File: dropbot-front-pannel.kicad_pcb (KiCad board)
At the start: 2 copper layers, 108.3 x 68.8 mm, 11 parts, among them J1 TFM-120-02-X-DH, J2 TFM-125-02-X-DH, J3 TFM-120-02-X-DH, P1 CONN_02X10, P2 CONN_02X25, P4 CONN_02X25, P6 CONN_02X25, P8 CONN_02X10, P9 CONN_01X03

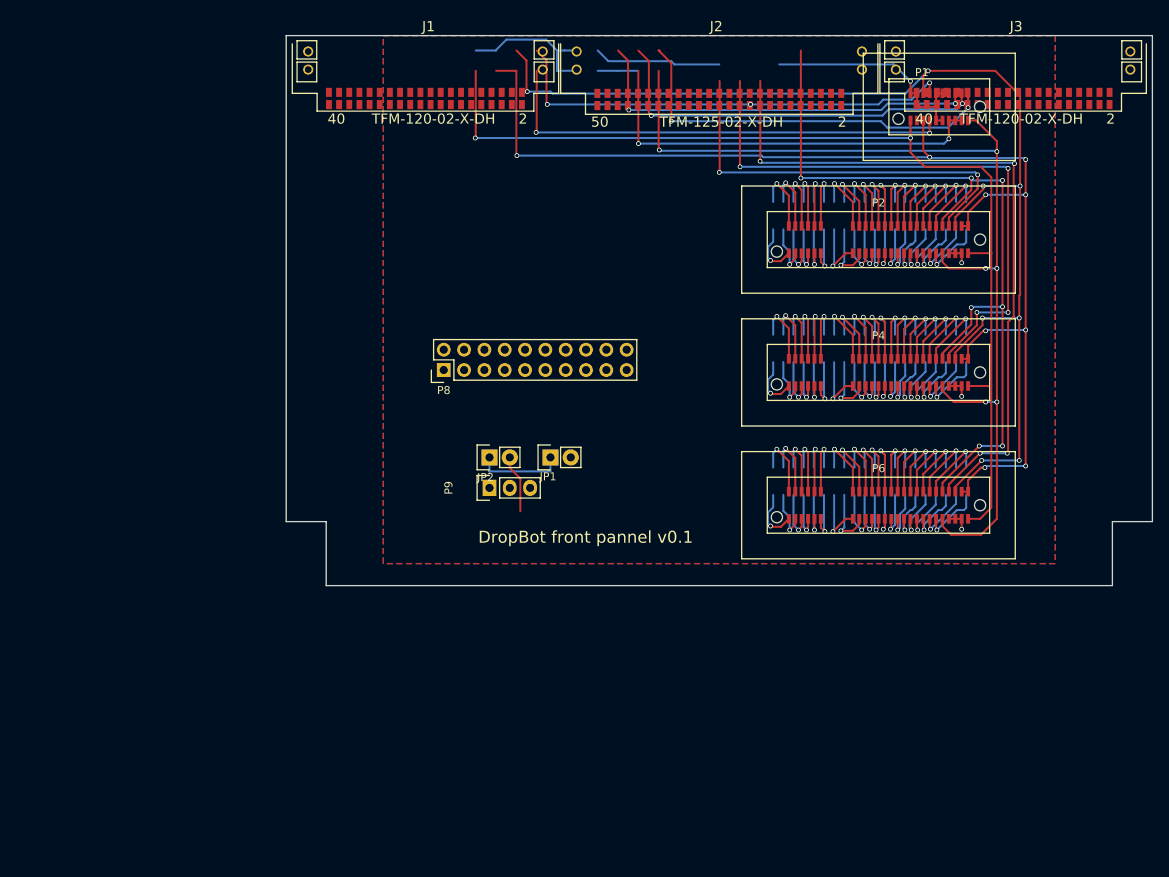
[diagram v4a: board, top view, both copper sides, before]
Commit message: [WIP] Update to use new Samtec connectors...
* add USB passthrough
* add 3.3V power regulator
* add reverse polarity protection on +12V power line
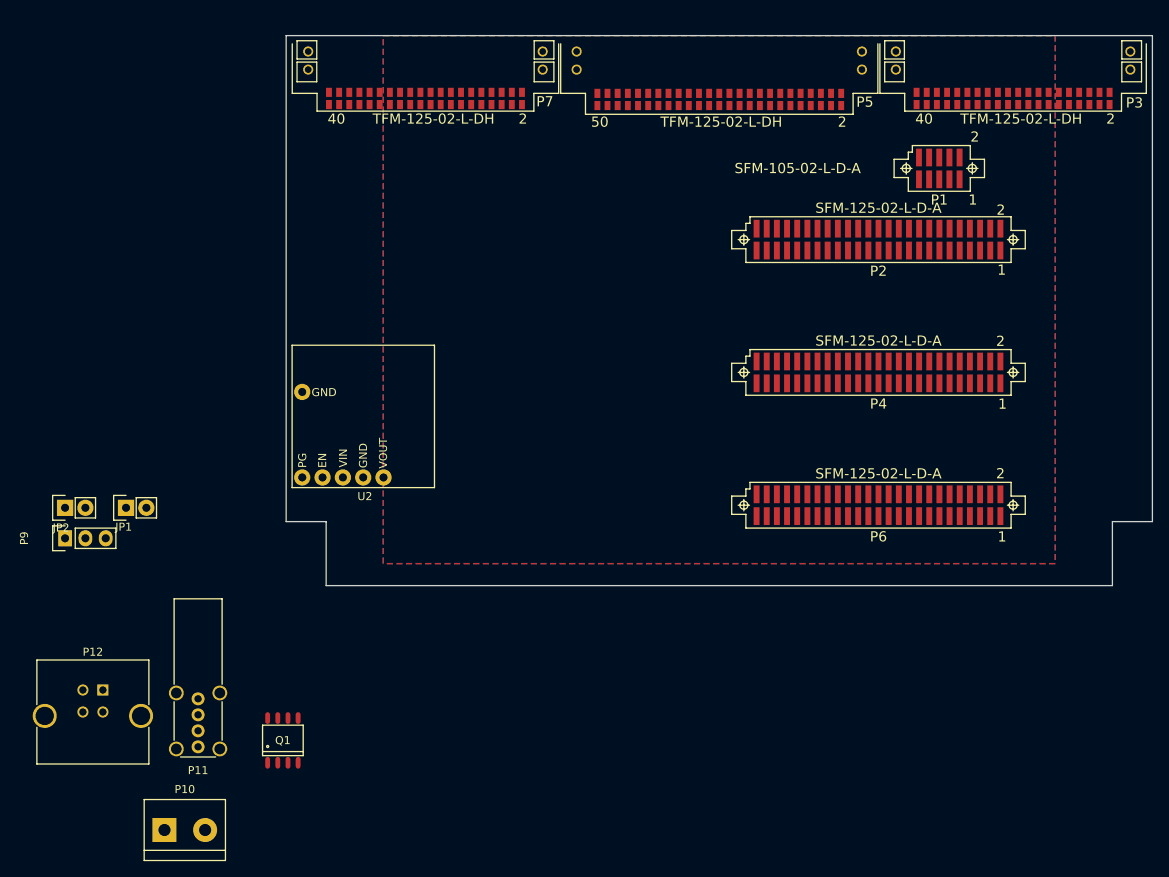
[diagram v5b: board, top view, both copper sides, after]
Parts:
- removed P8: CONN_02X10, Pin_Headers:Pin_Header_Straight_2x10
- added P10: CONN_01X02, Connect:bornier2, F.Cu at (-69.3, 120.3)
- added P11: USB_A, Connect:USB_A_Vertical, F.Cu at (-65.2, 103.9)
- added P12: USB_B, Connect:USB_B_MUSB_Straight, F.Cu at (-77.0, 102.8)
- added Q1: IRF9388TRPBF, Power_Integrations:SO-8, F.Cu at (-54.5, 109.1)
- added U2: D24V22F3, WheelerLab:D24V22F, F.Cu at (-53.4, 77.5)
- P1: value CONN_02X10 -> SFM-105-02-L-D-A; footprint WheelerLab:HSEC8-110-XX-X-DV -> WheelerLab:SFM-105-02-XXX-D-A
- P2, P4, P6: value CONN_02X25 -> SFM-125-02-L-D-A; footprint WheelerLab:HSEC8-125-XX-X-DV -> WheelerLab:SFM-125-02-XXX-D-A
- P3: renamed from J3; value TFM-120-02-X-DH -> TFM-125-02-L-DH
- P5: renamed from J2; value TFM-125-02-X-DH -> TFM-125-02-L-DH
- P7: renamed from J1; value TFM-120-02-X-DH -> TFM-125-02-L-DH
- moved JP1 53.4 mm to (-74.2, 80.0)
- moved JP2 53.4 mm to (-81.8, 80.0)
- moved P9 53.4 mm to (-81.8, 83.8)
- moved P1 7.70 mm to (27.5, 37.6)
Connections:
- P1 pad 10: GND -> HVAC
- P1 pad 4: GND -> SCL
- P1 pad 5: +3.3V -> CUR_SENSE
- P1 pad 6: SCL -> GND
- P1 pad 7: CUR_SENSE -> +12V
- P1 pad 9: GND -> +12V
- P3 pad 1: Net-(J3-Pad1) -> HVOUT0
- P3 pad 10: Net-(J3-Pad10) -> HVOUT9
- P3 pad 11: Net-(J3-Pad11) -> HVOUT10
- P3 pad 12: Net-(J3-Pad12) -> HVOUT11
- P3 pad 13: Net-(J3-Pad13) -> HVOUT12
- P3 pad 14: Net-(J3-Pad14) -> HVOUT13
- P3 pad 15: Net-(J3-Pad15) -> HVOUT14
- P3 pad 16: Net-(J3-Pad16) -> HVOUT15
- P3 pad 17: Net-(J3-Pad17) -> HVOUT16
- P3 pad 18: Net-(J3-Pad18) -> HVOUT17
- P3 pad 19: Net-(J3-Pad19) -> HVOUT18
- P3 pad 2: Net-(J3-Pad2) -> HVOUT1
- P3 pad 20: Net-(J3-Pad20) -> HVOUT19
- P3 pad 21: Net-(J3-Pad21) -> HVOUT20
- P3 pad 22: Net-(J3-Pad22) -> HVOUT21
- P3 pad 23: Net-(J3-Pad23) -> HVOUT22
- P3 pad 24: Net-(J3-Pad24) -> HVOUT23
- P3 pad 25: Net-(J3-Pad25) -> HVOUT24
- P3 pad 26: Net-(J3-Pad26) -> HVOUT25
- P3 pad 27: Net-(J3-Pad27) -> HVOUT26
- P3 pad 28: Net-(J3-Pad28) -> HVOUT27
- P3 pad 29: Net-(J3-Pad29) -> HVOUT28
- P3 pad 3: Net-(J3-Pad3) -> HVOUT2
- P3 pad 30: Net-(J3-Pad30) -> HVOUT29
- P3 pad 31: Net-(J3-Pad31) -> HVOUT30
- P3 pad 32: Net-(J3-Pad32) -> HVOUT31
- P3 pad 33: Net-(J3-Pad33) -> HVOUT32
- P3 pad 34: Net-(J3-Pad34) -> HVOUT33
- P3 pad 35: Net-(J3-Pad35) -> HVOUT34
- P3 pad 36: Net-(J3-Pad36) -> HVOUT35
- P3 pad 37: Net-(J3-Pad37) -> HVOUT36
- P3 pad 38: Net-(J3-Pad38) -> HVOUT37
- P3 pad 39: Net-(J3-Pad39) -> HVOUT38
- P3 pad 4: Net-(J3-Pad4) -> HVOUT3
- P3 pad 40: Net-(J3-Pad40) -> HVOUT39
- P3 pad 5: Net-(J3-Pad5) -> HVOUT4
- P3 pad 6: Net-(J3-Pad6) -> HVOUT5
- P3 pad 7: Net-(J3-Pad7) -> HVOUT6
- P3 pad 8: Net-(J3-Pad8) -> HVOUT7
- P3 pad 9: Net-(J3-Pad9) -> HVOUT8
- P5 pad 1: Net-(J2-Pad1) -> HVOUT40
- P5 pad 10: Net-(J2-Pad10) -> HVOUT49
- P5 pad 11: Net-(J2-Pad11) -> HVOUT50
- P5 pad 12: Net-(J2-Pad12) -> HVOUT51
- P5 pad 13: Net-(J2-Pad13) -> HVOUT52
- P5 pad 14: Net-(J2-Pad14) -> HVOUT53
- P5 pad 15: Net-(J2-Pad15) -> HVOUT54
- P5 pad 16: Net-(J2-Pad16) -> HVOUT55
- P5 pad 17: Net-(J2-Pad17) -> HVOUT56
- P5 pad 18: Net-(J2-Pad18) -> HVOUT57
- P5 pad 19: Net-(J2-Pad19) -> HVOUT58
- P5 pad 2: Net-(J2-Pad2) -> HVOUT41
- P5 pad 20: Net-(J2-Pad20) -> HVOUT59
- P5 pad 21: Net-(J2-Pad21) -> HVOUT60
- P5 pad 22: Net-(J2-Pad22) -> HVOUT61
- P5 pad 23: Net-(J2-Pad23) -> HVOUT62
- P5 pad 24: Net-(J2-Pad24) -> HVOUT63
- P5 pad 25: Net-(J2-Pad25) -> HVOUT64
- P5 pad 26: Net-(J2-Pad26) -> HVOUT65
- P5 pad 27: Net-(J2-Pad27) -> HVOUT66
- P5 pad 28: Net-(J2-Pad28) -> HVOUT67
- P5 pad 29: Net-(J2-Pad29) -> HVOUT68
- P5 pad 3: Net-(J2-Pad3) -> HVOUT42
- P5 pad 30: Net-(J2-Pad30) -> HVOUT69
- P5 pad 31: Net-(J2-Pad31) -> HVOUT70
- P5 pad 32: Net-(J2-Pad32) -> HVOUT71
- P5 pad 33: Net-(J2-Pad33) -> HVOUT72
- P5 pad 34: Net-(J2-Pad34) -> HVOUT73
- P5 pad 35: Net-(J2-Pad35) -> HVOUT74
- P5 pad 36: Net-(J2-Pad36) -> HVOUT75
- P5 pad 37: Net-(J2-Pad37) -> HVOUT76
- P5 pad 38: Net-(J2-Pad38) -> HVOUT77
- P5 pad 39: Net-(J2-Pad39) -> HVOUT78
- P5 pad 4: Net-(J2-Pad4) -> HVOUT43
- P5 pad 40: Net-(J2-Pad40) -> HVOUT79
- P5 pad 5: Net-(J2-Pad5) -> HVOUT44
- P5 pad 6: Net-(J2-Pad6) -> HVOUT45
- P5 pad 7: Net-(J2-Pad7) -> HVOUT46
- P5 pad 8: Net-(J2-Pad8) -> HVOUT47
- P5 pad 9: Net-(J2-Pad9) -> HVOUT48
- P7 pad 1: Net-(J1-Pad1) -> HVOUT80
- P7 pad 10: Net-(J1-Pad10) -> HVOUT89
- P7 pad 11: Net-(J1-Pad11) -> HVOUT90
- P7 pad 12: Net-(J1-Pad12) -> HVOUT91
- P7 pad 13: Net-(J1-Pad13) -> HVOUT92
- P7 pad 14: Net-(J1-Pad14) -> HVOUT93
- P7 pad 15: Net-(J1-Pad15) -> HVOUT94
- P7 pad 16: Net-(J1-Pad16) -> HVOUT95
- P7 pad 17: Net-(J1-Pad17) -> HVOUT96
- P7 pad 18: Net-(J1-Pad18) -> HVOUT97
- P7 pad 19: Net-(J1-Pad19) -> HVOUT98
- P7 pad 2: Net-(J1-Pad2) -> HVOUT81
- P7 pad 20: Net-(J1-Pad20) -> HVOUT99
- P7 pad 21: Net-(J1-Pad21) -> HVOUT100
- P7 pad 22: Net-(J1-Pad22) -> HVOUT101
- P7 pad 23: Net-(J1-Pad23) -> HVOUT102
- P7 pad 24: Net-(J1-Pad24) -> HVOUT103
- P7 pad 25: Net-(J1-Pad25) -> HVOUT104
- P7 pad 26: Net-(J1-Pad26) -> HVOUT105
- P7 pad 27: Net-(J1-Pad27) -> HVOUT106
- P7 pad 28: Net-(J1-Pad28) -> HVOUT107
- P7 pad 29: Net-(J1-Pad29) -> HVOUT108
- P7 pad 3: Net-(J1-Pad3) -> HVOUT82
- P7 pad 30: Net-(J1-Pad30) -> HVOUT109
- P7 pad 31: Net-(J1-Pad31) -> HVOUT110
- P7 pad 32: Net-(J1-Pad32) -> HVOUT111
- P7 pad 33: Net-(J1-Pad33) -> HVOUT112
- P7 pad 34: Net-(J1-Pad34) -> HVOUT113
- P7 pad 35: Net-(J1-Pad35) -> HVOUT114
- P7 pad 36: Net-(J1-Pad36) -> HVOUT115
- P7 pad 37: Net-(J1-Pad37) -> HVOUT116
- P7 pad 38: Net-(J1-Pad38) -> HVOUT117
- P7 pad 39: Net-(J1-Pad39) -> HVOUT118
- P7 pad 4: Net-(J1-Pad4) -> HVOUT83
- P7 pad 40: Net-(J1-Pad40) -> HVOUT119
- P7 pad 5: Net-(J1-Pad5) -> HVOUT84
- P7 pad 6: Net-(J1-Pad6) -> HVOUT85
- P7 pad 7: Net-(J1-Pad7) -> HVOUT86
- P7 pad 8: Net-(J1-Pad8) -> HVOUT87
- P7 pad 9: Net-(J1-Pad9) -> HVOUT88
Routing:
- net +3.3V: track 152.2 -> 0.00 mm, vias 9 -> 0
- net SCL: track 130.4 -> 0.00 mm, vias 7 -> 0
- net HVAC: track 129.3 -> 0.00 mm, vias 6 -> 0
- net SDA: track 129.0 -> 0.00 mm, vias 2 -> 0
- net HVGND: track 104.4 -> 0.00 mm, vias 7 -> 0
- net RST3: track 88.4 -> 0.00 mm, vias 4 -> 0
- net RST2: track 73.5 -> 0.00 mm, vias 4 -> 0
- net CUR_SENSE: track 58.6 -> 0.00 mm, vias 2 -> 0
- net Net-(J2-Pad20): track 56.2 -> 0.00 mm, vias 3 -> 0
- net +12V: track 52.1 -> 0.00 mm, vias 2 -> 0
- net RST1: track 51.8 -> 0.00 mm, vias 2 -> 0
- net D+: track 49.7 -> 0.00 mm, vias 2 -> 0
- net Net-(P5-Pad44): track 49.1 -> 0.00 mm, vias 1 -> 0
- net Net-(J3-Pad30): track 48.2 -> 0.00 mm, vias 2 -> 0
- net GND: track 45.3 -> 0.00 mm, vias 4 -> 0
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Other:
- board text added: "DropBot front pannel v0.2"
- board text removed: "DropBot front pannel v0.1"

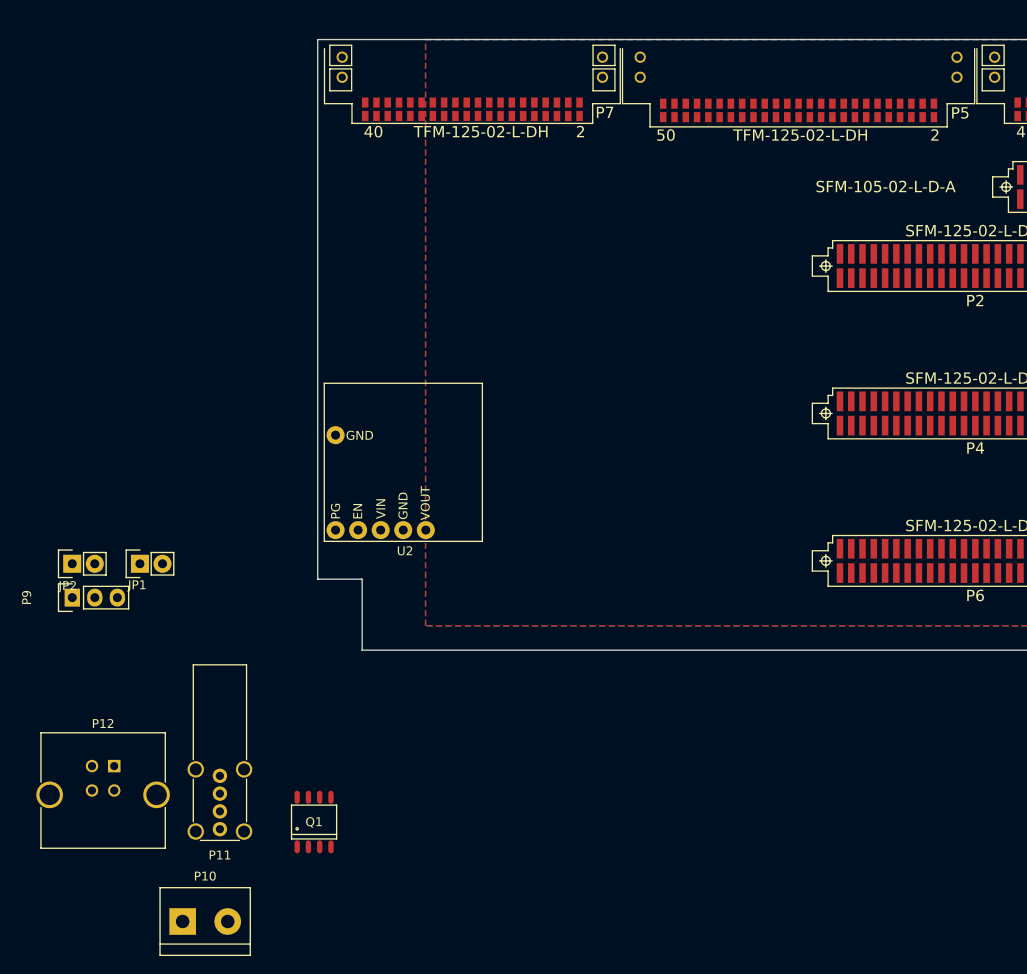
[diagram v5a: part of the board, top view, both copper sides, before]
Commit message: [WIP] update USB parts, replace jumpers with 0805 pads
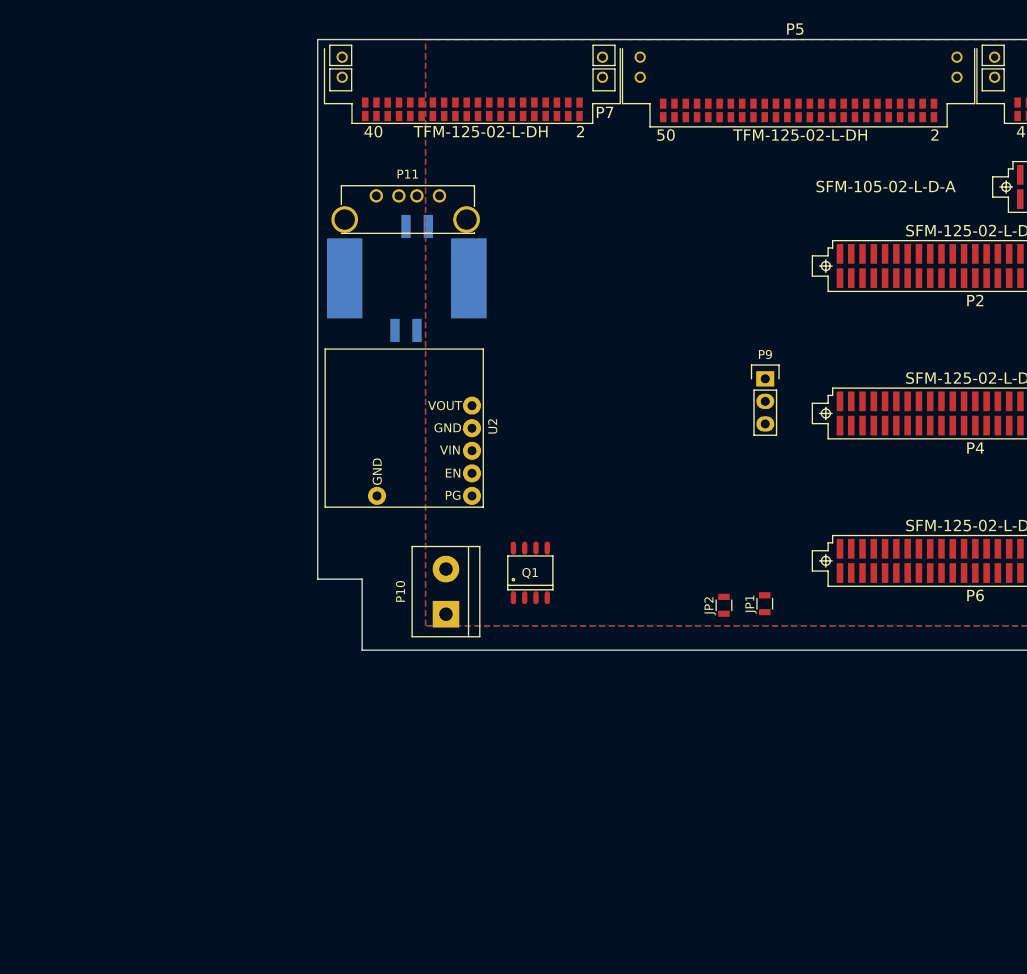
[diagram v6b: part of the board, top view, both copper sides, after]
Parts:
- JP1, JP2: footprint Pin_Headers:Pin_Header_Straight_1x02 -> Resistors_SMD:R_0805
- P11: footprint Connect:USB_A_Vertical -> WheelerLab:UE27AE54100
- P12: footprint Connect:USB_B_MUSB_Straight -> WheelerLab:1734517-1; moved to B.Cu
- moved P9 81.8 mm to (-3.75, 59.2), turned to 0 degrees
- moved JP2 73.5 mm to (-8.40, 84.7)
- moved JP1 70.5 mm to (-3.81, 84.5)
- moved P11 68.6 mm to (-44.0, 38.6)
- moved P12 64.3 mm to (-43.6, 47.9)
- moved P10 45.6 mm to (-39.7, 85.7), turned to 90 degrees
- moved Q1 37.1 mm to (-30.2, 81.0)
- moved U2 18.3 mm to (-35.5, 73.7), turned to 90 degrees
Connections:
- P3 pad G2: Net-(P3-PadG2) -> Net-(P3-PadG1)
- P3 pad G3: Net-(P3-PadG3) -> Net-(P3-PadG1)
- P3 pad G4: Net-(P3-PadG4) -> Net-(P3-PadG1)
- P7 pad G2: Net-(P7-PadG2) -> Net-(P7-PadG1)
- P7 pad G3: Net-(P7-PadG3) -> Net-(P7-PadG1)
- P7 pad G4: Net-(P7-PadG4) -> Net-(P7-PadG1)
